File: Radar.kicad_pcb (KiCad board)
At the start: 4 copper layers, 112 parts, among them J1 Receive_Antenna, J10 Conn_Coaxial, J11 Conn_02x05_Odd_Even, J12 supply rails, J2 VCO_Tune, J3 Transmit Antenna, J4 Output, J5 Conn_Coaxial, J6 Conn_Coaxial, J7 Conn_Coaxial, J8 Conn_Coaxial, J9 Conn_Coaxial, U10 AD5252, U11 LT1722, U12 AD8039, U13 PMA-63GLN+, U14 QPC6324, U15 PMA-63GLN+, U16 QPC6324, U17 HMC218BMS8GE, U18 AZ1117-5.0, U19 RP117, U20 MIC5317, U21 L78L33_SO8, U23 HMC430, U24 RFPA5542

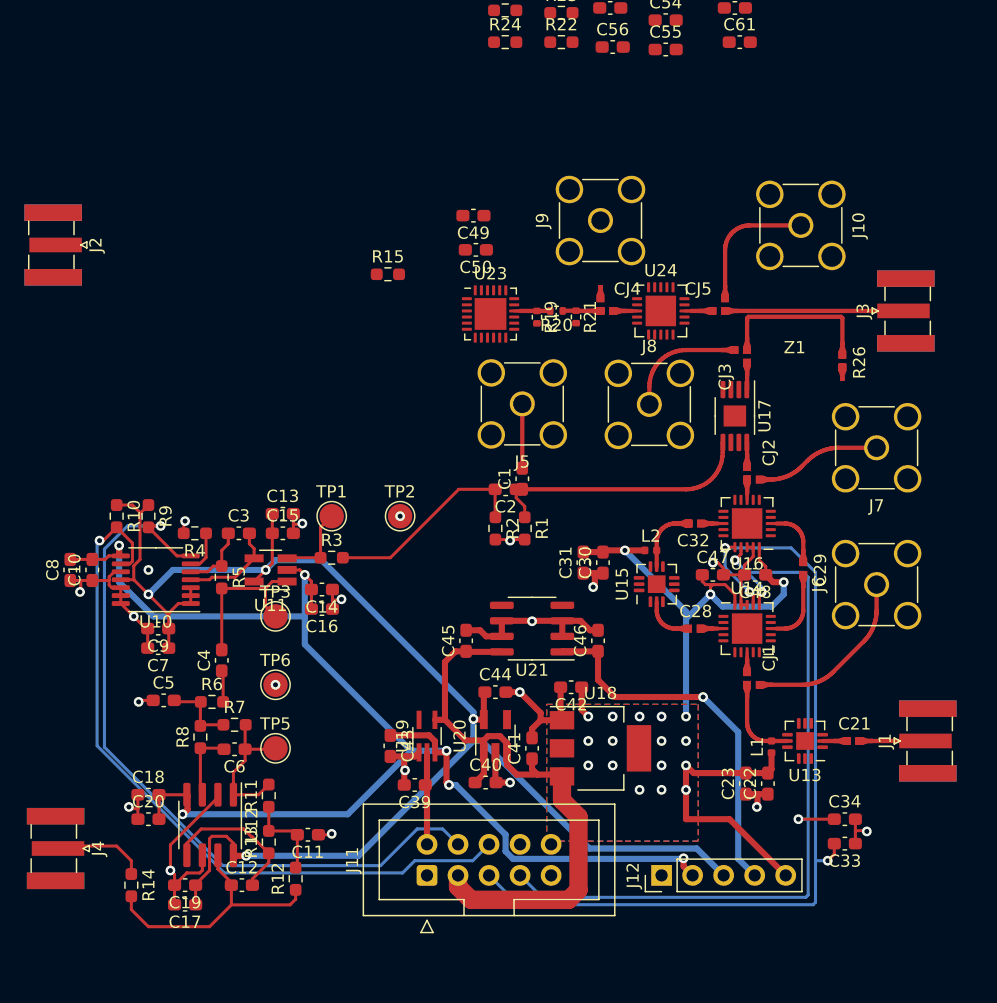
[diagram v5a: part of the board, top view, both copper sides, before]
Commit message: Added RX shield
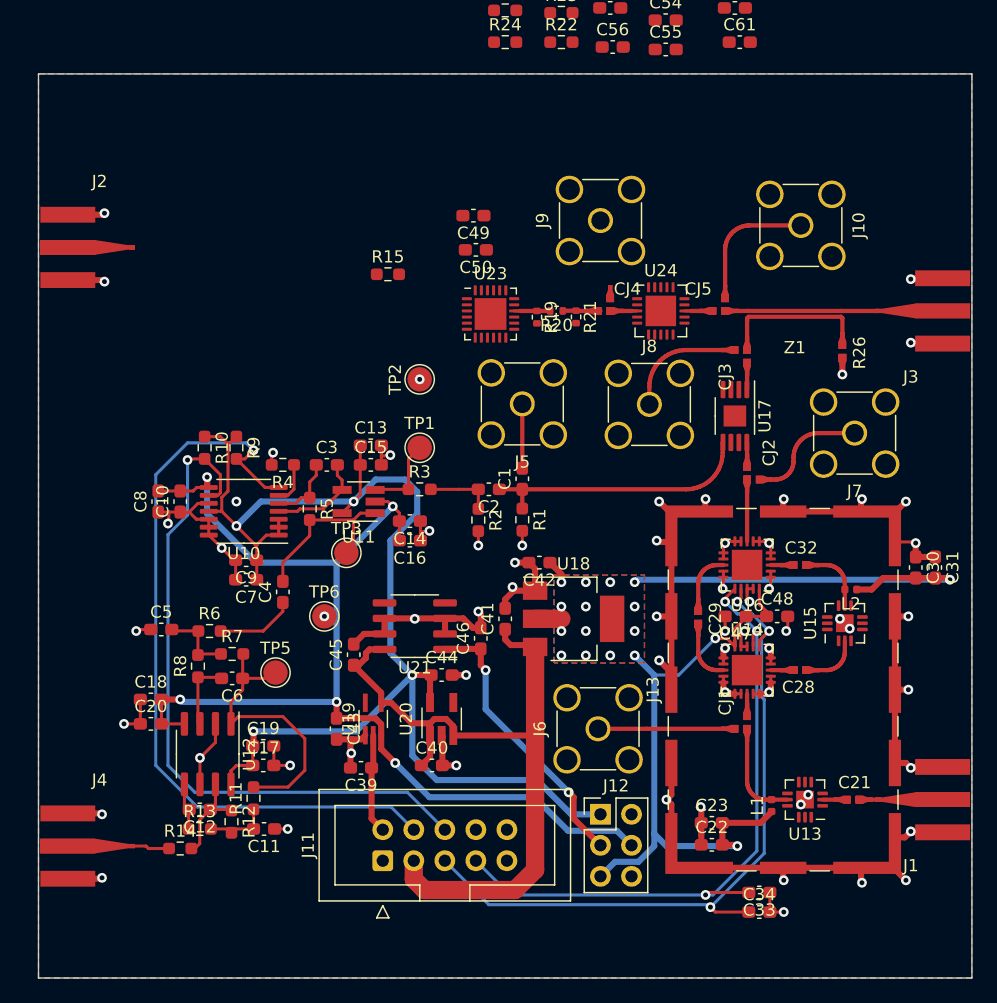
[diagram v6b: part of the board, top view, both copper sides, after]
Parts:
- added J13: RF_Shield_Two_Pieces, RF_Shielding:Laird_Technologies_BMI-S-209-F_29.36x18.50mm, F.Cu at (164.9, 75.8)
- J1, J2, J3, J4: footprint own:SMA_ADAM_TECH_edge_mount -> own:SMA_ADAM_TECH_edge
- J12: value supply rails -> Conn_02x03_Odd_Even; footprint Connector_PinHeader_2.54mm:PinHeader_1x05_P2.54mm_Vertical -> Connector_PinHeader_2.54mm:PinHeader_2x03_P2.54mm_Vertical
- moved C31 28.8 mm to (177.4, 65.8), turned to 270 degrees
- moved J6 25.7 mm to (149.8, 79.0)
- moved C30 25.6 mm to (175.8, 65.8), turned to 270 degrees
- moved L2 16.7 mm to (170.5, 67.6), turned to 180 degrees
- moved U15 15.7 mm to (170.0, 70.4)
- moved C17 13.1 mm to (122.4, 82.0), turned to 0 degrees
- moved C19 13.1 mm to (122.4, 80.4), turned to 0 degrees
- moved TP2 11.3 mm to (135.2, 50.4), turned to 90 degrees
- moved C41 10.8 mm to (142.2, 70.0)
- moved U18 10.8 mm to (147.8, 70.0)
- moved C42 10.5 mm to (145.0, 65.4)
- moved C34 10.3 mm to (163.0, 94.0)
- moved C32 10.2 mm to (166.8, 65.6), turned to 0 degrees
- moved C46 9.60 mm to (140.2, 71.6)
- moved U21 9.60 mm to (134.8, 70.6)
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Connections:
- J11 pad 5: /Connector/SW_CTR1 -> /Connector/SW_CTR2
- J11 pad 7: /Connector/SW_CTR2 -> /Connector/SW_CTR1
- J12 pad 1: GND -> +2V5
- J12 pad 2: -2V5 -> GND
- J12 pad 3: +2V5 -> +3V3
- J12 pad 4: +3V3 -> -2V5
- U14 pad 13: Net-(C29-Pad1) -> Net-(C28-Pad1)
- U14 pad 3: Net-(C28-Pad1) -> Net-(C29-Pad1)
- U16 pad 13: Net-(C32-Pad2) -> Net-(C29-Pad2)
- U16 pad 3: Net-(C29-Pad2) -> Net-(C32-Pad2)
- U21 pad 4: Net-(U21-Pad4) -> (no net)
- U21 pad 5: Net-(U21-Pad5) -> (no net)
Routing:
- net GND: track 92.3 -> 194.0 mm, vias 21 -> 64
- net +5V: track 66.8 -> 90.1 mm, vias 19 -> 17
- net /Connector/SW_CTR1: track 72.1 -> 53.6 mm
- net -2V5: track 110.4 -> 92.8 mm, vias 6 -> 5
- net +2V5: track 122.5 -> 108.4 mm
- net Net-(C12-Pad1): track 21.3 -> 8.01 mm
- net Net-(C2-Pad2): track 17.1 -> 5.49 mm
- net Net-(C6-Pad1): track 11.9 -> 23.4 mm
- net +6V: track 50.1 -> 59.9 mm
- net Net-(C12-Pad2): track 12.2 -> 3.83 mm
- net +3V3: track 30.8 -> 23.1 mm, vias 1 -> 2
- net /Connector/SW_CTR2: track 65.2 -> 57.9 mm
- net /Connector/SCL: track 60.4 -> 56.3 mm
- net Net-(C4-Pad1): track 2.58 -> 6.49 mm
- net Net-(CJ1-Pad3): track 14.8 -> 11.2 mm
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- added copper zone on B.Cu, net GND
- added copper zone on F.Cu, net GND
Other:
- board outline added: 76.4 x 74 mm
- net class Power added: clearance 0.09, trace_width 0.5, via_dia 0.8, via_drill 0.4

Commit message: Finished TX layout
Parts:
- C55, C57, C61: footprint Capacitor_SMD:C_0603_1608Metric_Pad1.08x0.95mm_HandSolder -> Capacitor_SMD:C_0402_1005Metric_Pad0.74x0.62mm_HandSolder
- moved R25 46.2 mm to (152.5, 65.2), turned to 180 degrees
- moved C59 45.2 mm to (152.5, 62.0)
- moved R23 44.9 mm to (148.8, 65.2)
- moved C53 43.9 mm to (148.8, 62.0), turned to 180 degrees
- moved R24 42.0 mm to (152.5, 63.5)
- moved R22 40.7 mm to (148.8, 63.5), turned to 180 degrees
- moved C57 21.6 mm to (156.1, 40.9), turned to 90 degrees
- moved C60 20.4 mm to (157.7, 40.1), turned to 90 degrees
- moved C61 19.3 mm to (154.8, 40.9), turned to 90 degrees
- moved C55 17.6 mm to (153.6, 40.9), turned to 90 degrees
- moved C54 16.8 mm to (155.6, 37.8), turned to 90 degrees
- moved C56 14.9 mm to (153.9, 37.8), turned to 90 degrees
- moved R15 8.74 mm to (140.8, 38.8), turned to 90 degrees
- moved C49 5.65 mm to (143.9, 40.7), turned to 90 degrees
- moved C50 2.75 mm to (142.4, 40.7), turned to 90 degrees
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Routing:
- net +5V: track 90.1 -> 150.5 mm, vias 17 -> 20
- net +3V3: track 23.1 -> 67.5 mm, vias 2 -> 3
- net /Connector/PDET: track 0.00 -> 38.8 mm, vias 0 -> 1
- net /Transmitter/VCO_TUNE_IN: track 0.00 -> 32.6 mm
- net GND: track 194.0 -> 225.8 mm, vias 64 -> 89
- net /Connector/PA_EN: track 0.00 -> 29.9 mm, vias 0 -> 2
- net Net-(C59-Pad1): track 0.00 -> 23.9 mm, vias 0 -> 2
- net Net-(C53-Pad1): track 0.00 -> 23.3 mm, vias 0 -> 2
- net Net-(CJ4-Pad3): track 0.00 -> 6.67 mm
- net /ReceiverIF/IF_OUT: track 7.92 -> 6.05 mm
- net Net-(C12-Pad1): track 8.01 -> 9.30 mm
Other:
- net class RF: clearance 0.09 -> 0.15
- board text added: "TODO:EDGE MOUNT FOOTPRINT"

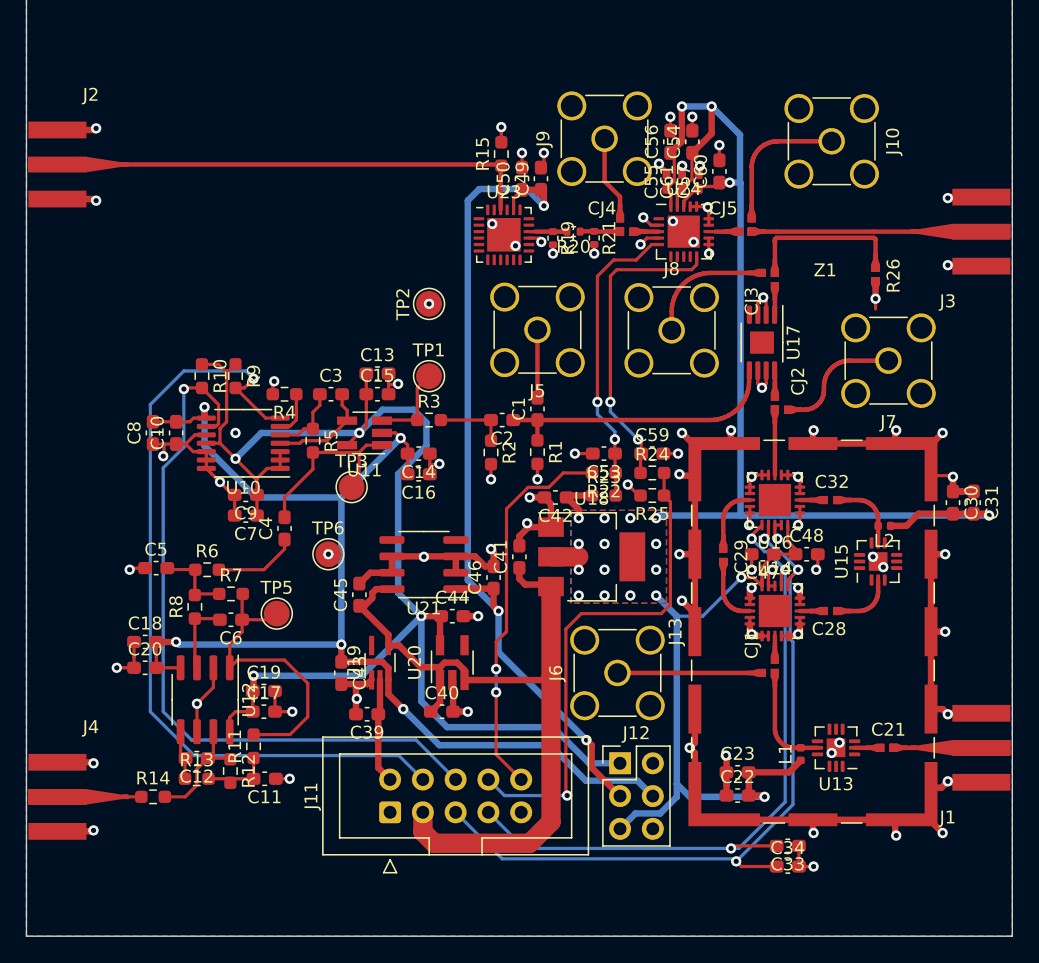
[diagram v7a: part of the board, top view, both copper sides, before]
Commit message: Removed soldermask from RF paths
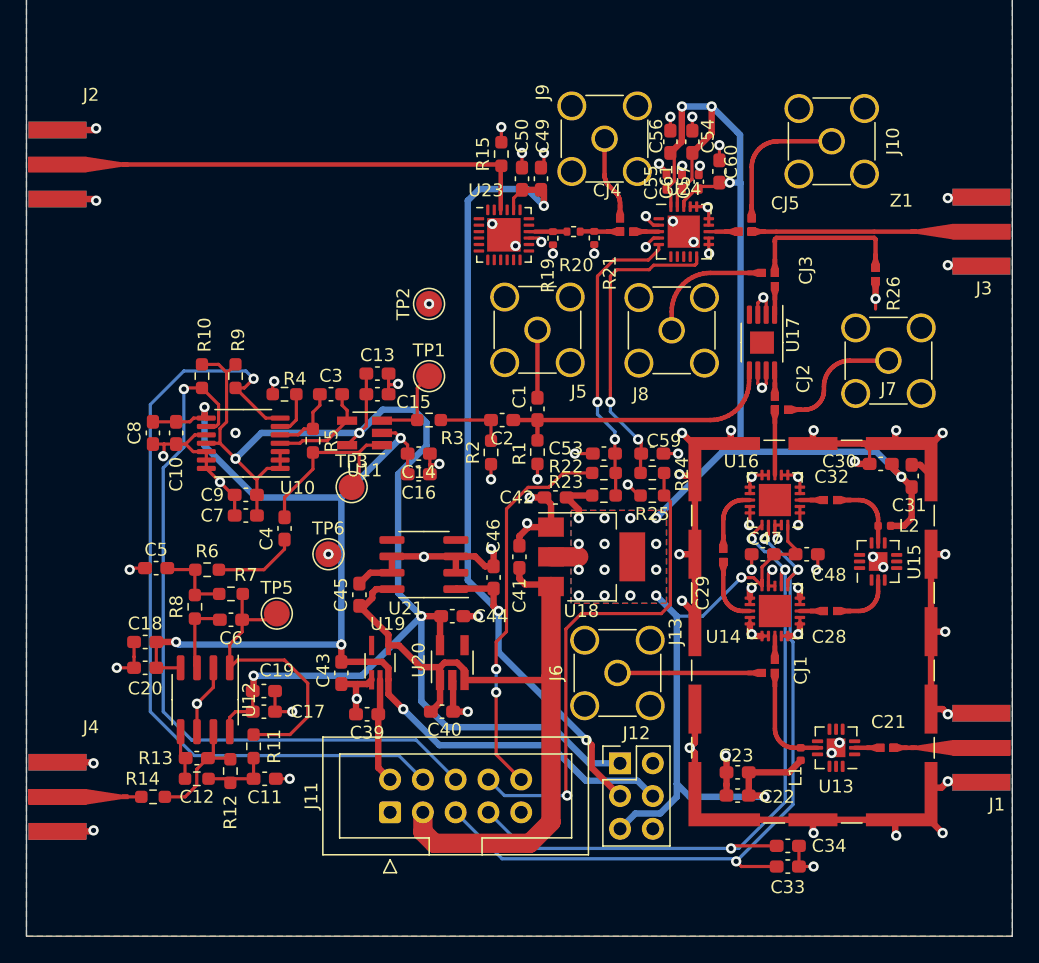
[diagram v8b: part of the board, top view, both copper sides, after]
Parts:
- moved C30 6.35 mm to (170.2, 62.8), turned to 0 degrees
- moved C31 5.22 mm to (172.6, 63.7)
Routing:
- net +5V: track 150.5 -> 140.5 mm
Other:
- board text removed: "TODO:EDGE MOUNT FOOTPRINT"
